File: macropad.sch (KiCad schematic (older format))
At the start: 62 parts, among them SW1 SW_PUSH, SW10 SW_PUSH, SW11 SW_PUSH, SW12 SW_PUSH, SW13 SW_PUSH, SW14 SW_PUSH, SW15 SW_PUSH, SW16 SW_PUSH, SW17 SW_PUSH, SW18 SW_PUSH, SW19 SW_PUSH, SW2 SW_PUSH, SW20 SW_PUSH, SW21 Rotary_Encoder_Switch, SW22 Rotary_Encoder_Switch, SW23 RESET_SWITCH, SW3 SW_PUSH, SW4 SW_PUSH, SW5 SW_PUSH, SW6 SW_PUSH, SW7 SW_PUSH, SW8 SW_PUSH, SW9 SW_PUSH, U1 ProMicro

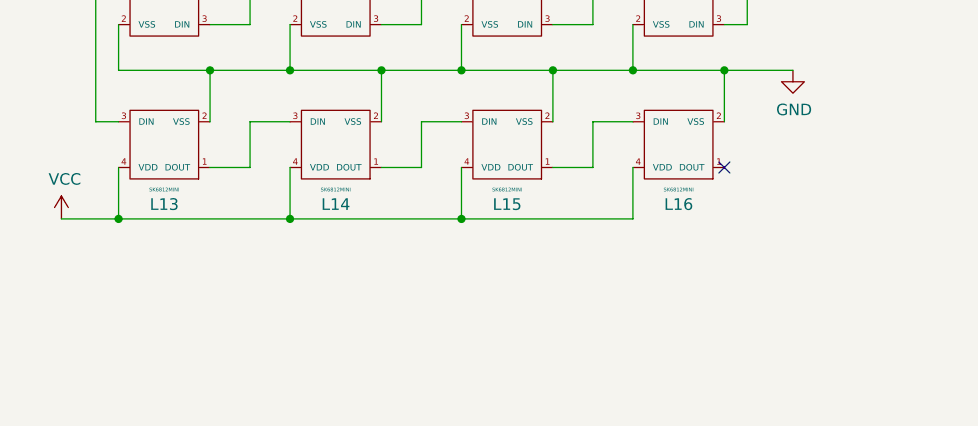
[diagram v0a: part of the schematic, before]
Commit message: add footprint placement and a bit of routing
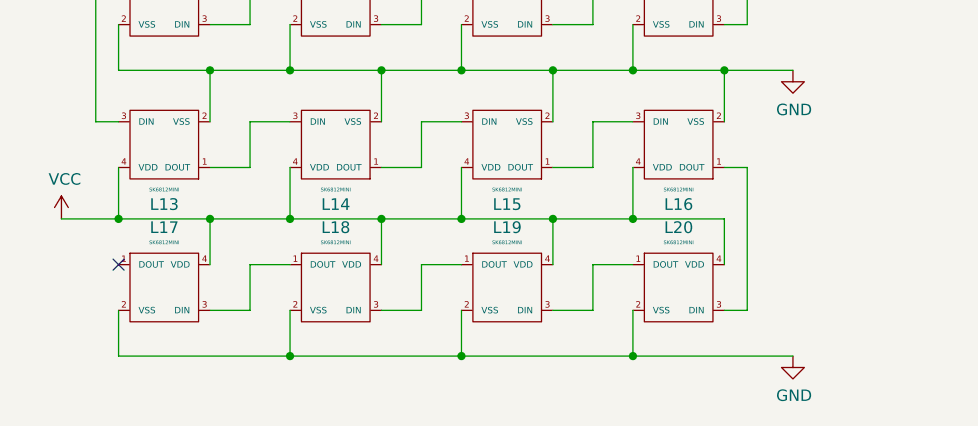
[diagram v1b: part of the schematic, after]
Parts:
- added L17, L18, L19, L20: SK6812MINI, kbd_Parts:LED_SK6812MINI-E_BL, symbol kbd:SK6812MINI
- SW1, SW10, SW11, SW12, SW13, SW14, SW15, SW16, SW17, SW18, SW19, SW2, SW20, SW3, SW4, SW5, SW6, SW7, SW8, SW9: footprint kbd_SW:CherryMX_Choc_Hotswap_1u -> kbd_SW:CherryMX_Hotswap_1.0u
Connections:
- net GND: now also L17.2 (VSS), L18.2 (VSS), L19.2 (VSS), L20.2 (VSS)
- net VCC: now also L17.4 (VDD), L18.4 (VDD), L19.4 (VDD), L20.4 (VDD)
- net at L16.1 (DOUT): now also L20.3 (DIN)
- new net: L17.3 (DIN), L18.1 (DOUT)
- new net: L18.3 (DIN), L19.1 (DOUT)
- new net: L19.3 (DIN), L20.1 (DOUT)
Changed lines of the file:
@@
 F 0 "SW1" H 7425 1455 50  0000 C CNN
 F 1 "SW_PUSH" H 7425 1364 50  0000 C CNN
-F 2 "kbd_SW:CherryMX_Choc_Hotswap_1u" H 7425 1200 50  0001 C CNN
+F 2 "kbd_SW:CherryMX_Hotswap_1.0u" H 7425 1200 50  0001 C CNN
 F 3 "" H 7425 1200 50  0000 C CNN
 	1    7425 1200
@@
 F 0 "SW2" H 8425 1455 50  0000 C CNN
 F 1 "SW_PUSH" H 8425 1364 50  0000 C CNN
-F 2 "kbd_SW:CherryMX_Choc_Hotswap_1u" H 8425 1200 50  0001 C CNN
+F 2 "kbd_SW:CherryMX_Hotswap_1.0u" H 8425 1200 50  0001 C CNN
 F 3 "" H 8425 1200 50  0000 C CNN
 	1    8425 1200
@@
 F 0 "SW3" H 9425 1455 50  0000 C CNN
 F 1 "SW_PUSH" H 9425 1364 50  0000 C CNN
-F 2 "kbd_SW:CherryMX_Choc_Hotswap_1u" H 9425 1200 50  0001 C CNN
+F 2 "kbd_SW:CherryMX_Hotswap_1.0u" H 9425 1200 50  0001 C CNN
 F 3 "" H 9425 1200 50  0000 C CNN
 	1    9425 1200
@@
 F 0 "SW4" H 10425 1455 50  0000 C CNN
 F 1 "SW_PUSH" H 10425 1364 50  0000 C CNN
-F 2 "kbd_SW:CherryMX_Choc_Hotswap_1u" H 10425 1200 50  0001 C CNN
+F 2 "kbd_SW:CherryMX_Hotswap_1.0u" H 10425 1200 50  0001 C CNN
 F 3 "" H 10425 1200 50  0000 C CNN
 	1    10425 1200
@@
 F 0 "SW5" H 7425 1955 50  0000 C CNN
 F 1 "SW_PUSH" H 7425 1864 50  0000 C CNN
-F 2 "kbd_SW:CherryMX_Choc_Hotswap_1u" H 7425 1700 50  0001 C CNN
+F 2 "kbd_SW:CherryMX_Hotswap_1.0u" H 7425 1700 50  0001 C CNN
 F 3 "" H 7425 1700 50  0000 C CNN
 	1    7425 1700
@@
 F 0 "SW6" H 8425 1955 50  0000 C CNN
 F 1 "SW_PUSH" H 8425 1864 50  0000 C CNN
-F 2 "kbd_SW:CherryMX_Choc_Hotswap_1u" H 8425 1700 50  0001 C CNN
+F 2 "kbd_SW:CherryMX_Hotswap_1.0u" H 8425 1700 50  0001 C CNN
 F 3 "" H 8425 1700 50  0000 C CNN
 	1    8425 1700
@@
 F 0 "SW7" H 9425 1955 50  0000 C CNN
 F 1 "SW_PUSH" H 9425 1864 50  0000 C CNN
-F 2 "kbd_SW:CherryMX_Choc_Hotswap_1u" H 9425 1700 50  0001 C CNN
+F 2 "kbd_SW:CherryMX_Hotswap_1.0u" H 9425 1700 50  0001 C CNN
 F 3 "" H 9425 1700 50  0000 C CNN
 	1    9425 1700
@@
 F 0 "SW8" H 10425 1955 50  0000 C CNN
 F 1 "SW_PUSH" H 10425 1864 50  0000 C CNN
-F 2 "kbd_SW:CherryMX_Choc_Hotswap_1u" H 10425 1700 50  0001 C CNN
+F 2 "kbd_SW:CherryMX_Hotswap_1.0u" H 10425 1700 50  0001 C CNN
 F 3 "" H 10425 1700 50  0000 C CNN
 	1    10425 1700
@@
 F 0 "SW9" H 7425 2455 50  0000 C CNN
 F 1 "SW_PUSH" H 7425 2364 50  0000 C CNN
-F 2 "kbd_SW:CherryMX_Choc_Hotswap_1u" H 7425 2200 50  0001 C CNN
+F 2 "kbd_SW:CherryMX_Hotswap_1.0u" H 7425 2200 50  0001 C CNN
 F 3 "" H 7425 2200 50  0000 C CNN
 	1    7425 2200
@@
 F 0 "SW10" H 8425 2455 50  0000 C CNN
 F 1 "SW_PUSH" H 8425 2364 50  0000 C CNN
-F 2 "kbd_SW:CherryMX_Choc_Hotswap_1u" H 8425 2200 50  0001 C CNN
+F 2 "kbd_SW:CherryMX_Hotswap_1.0u" H 8425 2200 50  0001 C CNN
 F 3 "" H 8425 2200 50  0000 C CNN
 	1    8425 2200
@@
 F 0 "SW11" H 9425 2455 50  0000 C CNN
 F 1 "SW_PUSH" H 9425 2364 50  0000 C CNN
-F 2 "kbd_SW:CherryMX_Choc_Hotswap_1u" H 9425 2200 50  0001 C CNN
+F 2 "kbd_SW:CherryMX_Hotswap_1.0u" H 9425 2200 50  0001 C CNN
 F 3 "" H 9425 2200 50  0000 C CNN
 	1    9425 2200
@@
 F 0 "SW12" H 10425 2455 50  0000 C CNN
 F 1 "SW_PUSH" H 10425 2364 50  0000 C CNN
-F 2 "kbd_SW:CherryMX_Choc_Hotswap_1u" H 10425 2200 50  0001 C CNN
+F 2 "kbd_SW:CherryMX_Hotswap_1.0u" H 10425 2200 50  0001 C CNN
 F 3 "" H 10425 2200 50  0000 C CNN
 	1    10425 2200
@@
 F 0 "SW13" H 7425 2955 50  0000 C CNN
 F 1 "SW_PUSH" H 7425 2864 50  0000 C CNN
-F 2 "kbd_SW:CherryMX_Choc_Hotswap_1u" H 7425 2700 50  0001 C CNN
+F 2 "kbd_SW:CherryMX_Hotswap_1.0u" H 7425 2700 50  0001 C CNN
 F 3 "" H 7425 2700 50  0000 C CNN
 	1    7425 2700
@@
 F 0 "SW14" H 8425 2955 50  0000 C CNN
 F 1 "SW_PUSH" H 8425 2864 50  0000 C CNN
-F 2 "kbd_SW:CherryMX_Choc_Hotswap_1u" H 8425 2700 50  0001 C CNN
+F 2 "kbd_SW:CherryMX_Hotswap_1.0u" H 8425 2700 50  0001 C CNN
 F 3 "" H 8425 2700 50  0000 C CNN
 	1    8425 2700
@@
 F 0 "SW15" H 9425 2955 50  0000 C CNN
 F 1 "SW_PUSH" H 9425 2864 50  0000 C CNN
-F 2 "kbd_SW:CherryMX_Choc_Hotswap_1u" H 9425 2700 50  0001 C CNN
+F 2 "kbd_SW:CherryMX_Hotswap_1.0u" H 9425 2700 50  0001 C CNN
 F 3 "" H 9425 2700 50  0000 C CNN
 	1    9425 2700
@@
 F 0 "SW16" H 10425 2955 50  0000 C CNN
 F 1 "SW_PUSH" H 10425 2864 50  0000 C CNN
-F 2 "kbd_SW:CherryMX_Choc_Hotswap_1u" H 10425 2700 50  0001 C CNN
+F 2 "kbd_SW:CherryMX_Hotswap_1.0u" H 10425 2700 50  0001 C CNN
 F 3 "" H 10425 2700 50  0000 C CNN
 	1    10425 2700
@@
 F 0 "SW17" H 7425 3455 50  0000 C CNN
 F 1 "SW_PUSH" H 7425 3364 50  0000 C CNN
-F 2 "kbd_SW:CherryMX_Choc_Hotswap_1u" H 7425 3200 50  0001 C CNN
+F 2 "kbd_SW:CherryMX_Hotswap_1.0u" H 7425 3200 50  0001 C CNN
 F 3 "" H 7425 3200 50  0000 C CNN
 	1    7425 3200
@@
 F 0 "SW18" H 8425 3455 50  0000 C CNN
 F 1 "SW_PUSH" H 8425 3364 50  0000 C CNN
-F 2 "kbd_SW:CherryMX_Choc_Hotswap_1u" H 8425 3200 50  0001 C CNN
+F 2 "kbd_SW:CherryMX_Hotswap_1.0u" H 8425 3200 50  0001 C CNN
 F 3 "" H 8425 3200 50  0000 C CNN
 	1    8425 3200
@@
 F 0 "SW19" H 9425 3455 50  0000 C CNN
 F 1 "SW_PUSH" H 9425 3364 50  0000 C CNN
-F 2 "kbd_SW:CherryMX_Choc_Hotswap_1u" H 9425 3200 50  0001 C CNN
+F 2 "kbd_SW:CherryMX_Hotswap_1.0u" H 9425 3200 50  0001 C CNN
 F 3 "" H 9425 3200 50  0000 C CNN
 	1    9425 3200
@@
 F 0 "SW20" H 10425 3455 50  0000 C CNN
 F 1 "SW_PUSH" H 10425 3364 50  0000 C CNN
-F 2 "kbd_SW:CherryMX_Choc_Hotswap_1u" H 10425 3200 50  0001 C CNN
+F 2 "kbd_SW:CherryMX_Hotswap_1.0u" H 10425 3200 50  0001 C CNN
 F 3 "" H 10425 3200 50  0000 C CNN
 	1    10425 3200
@@
 Wire Wire Line
 	3950 3450 3650 3450
-NoConn ~ 3650 5325
 $Comp
 L power:VCC #PWR06
@@
 Connection ~ 2500 5550
 Wire Wire Line
-	2500 5550 3250 5550
+	2500 5550 2900 5550
 Wire Wire Line
 	1750 5325 1750 5550
 Connection ~ 1750 5550
 Wire Wire Line
-	1750 5550 2500 5550
+	1750 5550 2150 5550
 Wire Wire Line
 	1000 5325 1000 5550
 Connection ~ 1000 5550
 Wire Wire Line
-	1000 5550 1750 5550
+	1000 5550 1400 5550
 Wire Wire Line
 	2900 4900 3250 4900
@@
 Text GLabel 2475 1800 2    50   Input ~ 0
 rotaryD
+$Comp
+L kbd:SK6812MINI L17
+U 1 1 6184890E
+P 1200 5850
+F 0 "L17" H 1200 6112 51  0000 C CNN
+F 1 "SK6812MINI" H 1200 6047 16  0000 C CNN
+F 2 "kbd_Parts:LED_SK6812MINI-E_BL" H 1200 5850 60  0001 C CNN
+F 3 "" H 1200 5850 60  0001 C CNN
+	1    1200 5850
+	1    0    0    -1
+$EndComp
+$Comp
+L kbd:SK6812MINI L18
+U 1 1 61849B3D
+P 1950 5850
+F 0 "L18" H 1950 6112 51  0000 C CNN
+F 1 "SK6812MINI" H 1950 6047 16  0000 C CNN
+F 2 "kbd_Parts:LED_SK6812MINI-E_BL" H 1950 5850 60  0001 C CNN
+F 3 "" H 1950 5850 60  0001 C CNN
+	1    1950 5850
+	1    0    0    -1
+$EndComp
+$Comp
+L kbd:SK6812MINI L19
+U 1 1 6184A8A5
+P 2700 5850
+F 0 "L19" H 2700 6112 51  0000 C CNN
+F 1 "SK6812MINI" H 2700 6047 16  0000 C CNN
+F 2 "kbd_Parts:LED_SK6812MINI-E_BL" H 2700 5850 60  0001 C CNN
+F 3 "" H 2700 5850 60  0001 C CNN
+	1    2700 5850
+	1    0    0    -1
+$EndComp
+$Comp
+L kbd:SK6812MINI L20
+U 1 1 6184B23E
+P 3450 5850
+F 0 "L20" H 3450 6112 51  0000 C CNN
+F 1 "SK6812MINI" H 3450 6047 16  0000 C CNN
+F 2 "kbd_Parts:LED_SK6812MINI-E_BL" H 3450 5850 60  0001 C CNN
+F 3 "" H 3450 5850 60  0001 C CNN
+	1    3450 5850
+	1    0    0    -1
+$EndComp
+$Comp
+L power:GND #PWR013
+U 1 1 618591B9
+P 3950 6150
+F 0 "#PWR013" H 3950 5900 50  0001 C CNN
+F 1 "GND" H 3955 5977 50  0000 C CNN
+F 2 "" H 3950 6150 50  0001 C CNN
+F 3 "" H 3950 6150 50  0001 C CNN
+	1    3950 6150
+	1    0    0    -1
+$EndComp
+Wire Wire Line
+	3650 5325 3750 5325
+Wire Wire Line
+	3750 5325 3750 5950
+Wire Wire Line
+	3750 5950 3650 5950
+Wire Wire Line
+	3250 5750 3075 5750
+Wire Wire Line
+	3075 5750 3075 5950
+Wire Wire Line
+	3075 5950 2900 5950
+Wire Wire Line
+	2500 5750 2325 5750
+Wire Wire Line
+	2325 5750 2325 5950
+Wire Wire Line
+	2325 5950 2150 5950
+Wire Wire Line
+	1750 5750 1575 5750
+Wire Wire Line
+	1575 5750 1575 5950
+Wire Wire Line
+	1575 5950 1400 5950
+NoConn ~ 1000 5750
+Wire Wire Line
+	1400 5750 1400 5550
+Connection ~ 1400 5550
+Wire Wire Line
+	1400 5550 1750 5550
+Wire Wire Line
+	2150 5750 2150 5550
+Connection ~ 2150 5550
+Wire Wire Line
+	2150 5550 2500 5550
+Wire Wire Line
+	2900 5750 2900 5550
+Connection ~ 2900 5550
+Wire Wire Line
+	2900 5550 3250 5550
+Wire Wire Line
+	3250 5550 3650 5550
+Wire Wire Line
+	3650 5550 3650 5750
+Connection ~ 3250 5550
+Wire Wire Line
+	3950 6150 3250 6150
+Wire Wire Line
+	1000 6150 1000 5950
+Wire Wire Line
+	1750 5950 1750 6150
+Connection ~ 1750 6150
+Wire Wire Line
+	1750 6150 1000 6150
+Wire Wire Line
+	2500 5950 2500 6150
+Connection ~ 2500 6150
+Wire Wire Line
+	2500 6150 1750 6150
+Wire Wire Line
+	3250 5950 3250 6150
+Connection ~ 3250 6150
+Wire Wire Line
+	3250 6150 2500 6150
 $EndSCHEMATC
